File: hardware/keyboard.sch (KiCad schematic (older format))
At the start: 37 parts, among them J1 USB_OTG, J10 PD5, J11 PD6, J12 PD7, J13 PE6, J14 PF0, J15 PF1, J16 PF4, J17 PF5, J18 PF6, J19 PF7, J2 PB5, J3 PB6, J4 PB7, J5 PC6, J6 PC7, J7 PD2, J8 PD3, J9 PD4, U1 ATMEGA32U4-AU, Y1 16MHz

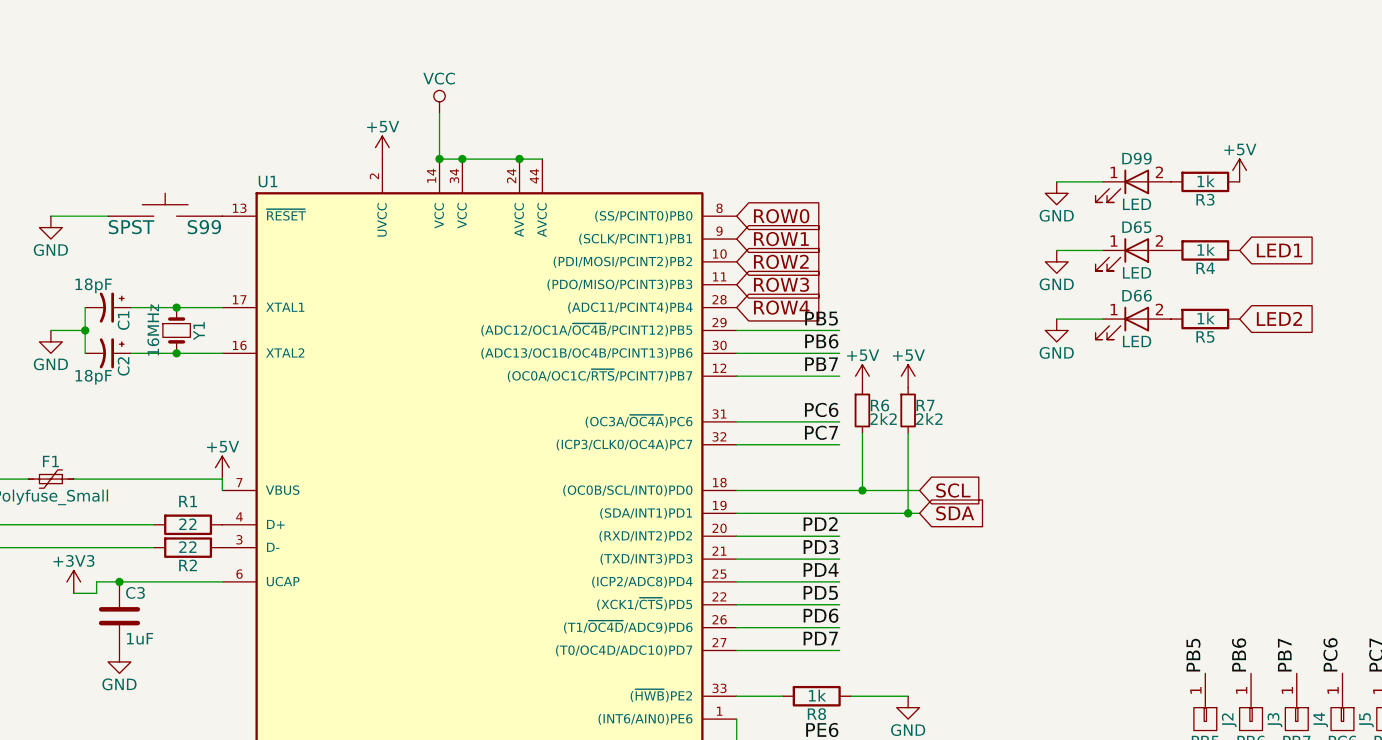
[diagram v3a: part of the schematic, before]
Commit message: Move diodes in script, add big thumb buttons
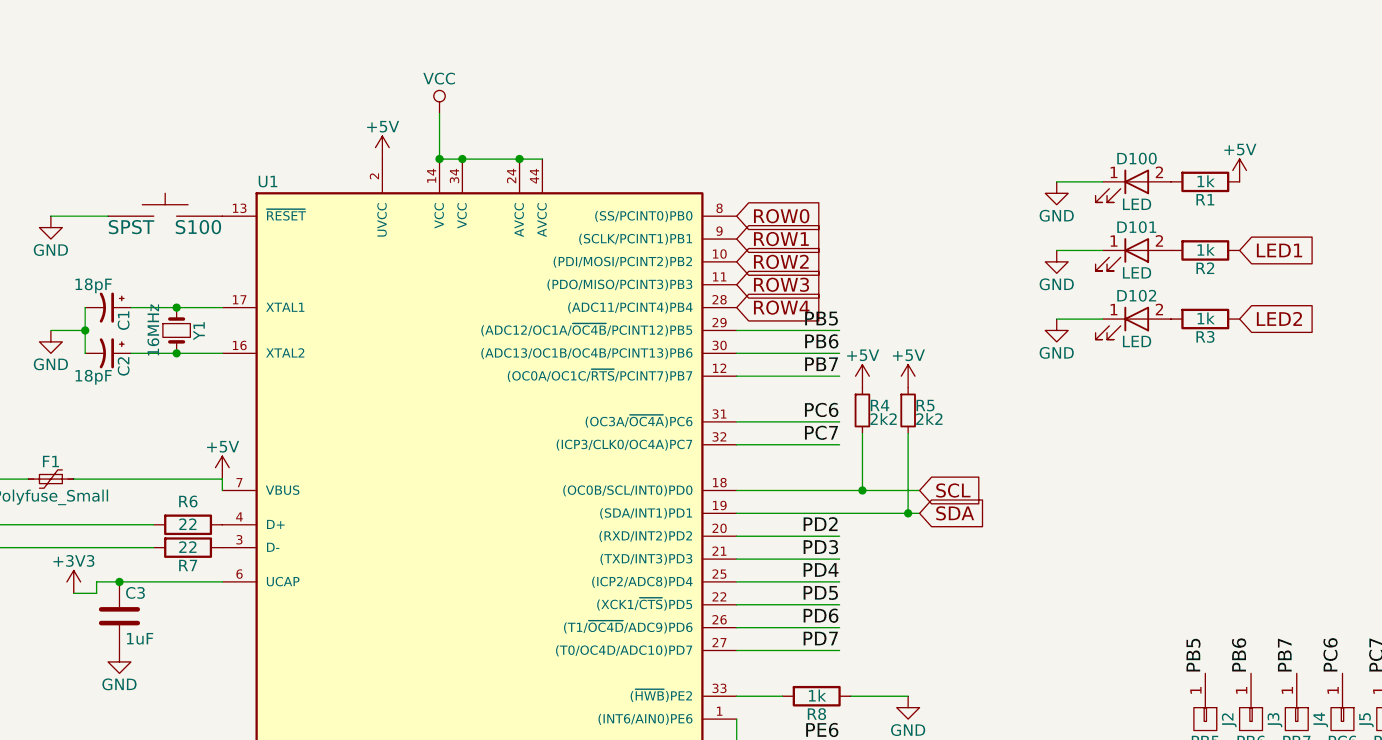
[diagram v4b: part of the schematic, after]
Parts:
- renumbered D99 to D100, D65 to D101, D66 to D102, R3 to R1, R4 to R2, R5 to R3, R6 to R4, R7 to R5, R1 to R6, R2 to R7, S99 to S100
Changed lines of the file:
@@
 $EndComp
 $Comp
-L R R1
+L R R6
 U 1 1 58E91E3A
 P 2650 2700
-F 0 "R1" V 2550 2700 50  0000 C CNN
+F 0 "R6" V 2550 2700 50  0000 C CNN
 F 1 "22" V 2650 2700 50  0000 C CNN
 F 2 "Resistors_SMD:R_1206_HandSoldering" V 2580 2700 50  0001 C CNN
@@
 $EndComp
 $Comp
-L R R2
+L R R7
 U 1 1 58E91EA1
 P 2650 2800
-F 0 "R2" V 2730 2800 50  0000 C CNN
+F 0 "R7" V 2730 2800 50  0000 C CNN
 F 1 "22" V 2650 2800 50  0000 C CNN
 F 2 "Resistors_SMD:R_1206_HandSoldering" V 2580 2800 50  0001 C CNN
@@
 $EndComp
 $Comp
-L LED D99
+L LED D100
 U 1 1 58EC6D5A
 P 6800 1200
-F 0 "D99" H 6800 1300 50  0000 C CNN
+F 0 "D100" H 6800 1300 50  0000 C CNN
 F 1 "LED" H 6800 1100 50  0000 C CNN
 F 2 "LEDs:LED_1206" H 6800 1200 50  0001 C CNN
@@
 $EndComp
 $Comp
-L R R3
+L R R1
 U 1 1 58EC77A9
 P 7100 1200
-F 0 "R3" V 7180 1200 50  0000 C CNN
+F 0 "R1" V 7180 1200 50  0000 C CNN
 F 1 "1k" V 7100 1200 50  0000 C CNN
 F 2 "Resistors_SMD:R_1206_HandSoldering" V 7030 1200 50  0001 C CNN
@@
 	5050 2550 5850 2550
 $Comp
-L R_Small R7
+L R_Small R5
 U 1 1 594E97F5
 P 5800 2200
-F 0 "R7" H 5830 2220 50  0000 L CNN
+F 0 "R5" H 5830 2220 50  0000 L CNN
 F 1 "2k2" H 5830 2160 50  0000 L CNN
 F 2 "Resistors_SMD:R_1206_HandSoldering" H 5800 2200 50  0001 C CNN
@@
 $EndComp
 $Comp
-L R_Small R6
+L R_Small R4
 U 1 1 594E9840
 P 5600 2200
-F 0 "R6" H 5630 2220 50  0000 L CNN
+F 0 "R4" H 5630 2220 50  0000 L CNN
 F 1 "2k2" H 5630 2160 50  0000 L CNN
 F 2 "Resistors_SMD:R_1206_HandSoldering" H 5600 2200 50  0001 C CNN
@@
 $EndComp
 $Comp
-L LED D65
+L LED D101
 U 1 1 594E9DFB
 P 6800 1500
-F 0 "D65" H 6800 1600 50  0000 C CNN
+F 0 "D101" H 6800 1600 50  0000 C CNN
 F 1 "LED" H 6800 1400 50  0000 C CNN
 F 2 "LEDs:LED_1206" H 6800 1500 50  0001 C CNN
@@
 $EndComp
 $Comp
-L R R4
+L R R2
 U 1 1 594E9E0D
 P 7100 1500
-F 0 "R4" V 7180 1500 50  0000 C CNN
+F 0 "R2" V 7180 1500 50  0000 C CNN
 F 1 "1k" V 7100 1500 50  0000 C CNN
 F 2 "Resistors_SMD:R_1206_HandSoldering" V 7030 1500 50  0001 C CNN
@@
 	6650 1500 6450 1500
 $Comp
-L LED D66
+L LED D102
 U 1 1 594E9E7C
 P 6800 1800
-F 0 "D66" H 6800 1900 50  0000 C CNN
+F 0 "D102" H 6800 1900 50  0000 C CNN
 F 1 "LED" H 6800 1700 50  0000 C CNN
 F 2 "LEDs:LED_1206" H 6800 1800 50  0001 C CNN
@@
 $EndComp
 $Comp
-L R R5
+L R R3
 U 1 1 594E9E8E
 P 7100 1800
-F 0 "R5" V 7180 1800 50  0000 C CNN
+F 0 "R3" V 7180 1800 50  0000 C CNN
 F 1 "1k" V 7100 1800 50  0000 C CNN
 F 2 "Resistors_SMD:R_1206_HandSoldering" V 7030 1800 50  0001 C CNN
@@
 $EndComp
 $Comp
-L SPST S99
+L SPST S100
 U 1 1 594EAF2A
 P 2550 1350
-F 0 "S99" H 2800 1300 60  0000 R CNN
+F 0 "S100" H 2800 1300 60  0000 R CNN
 F 1 "SPST" H 2400 1300 60  0000 C CNN
 F 2 "Buttons_Switches_SMD:SW_SPST_EVQP0" H 2550 1450 60  0001 C CNN

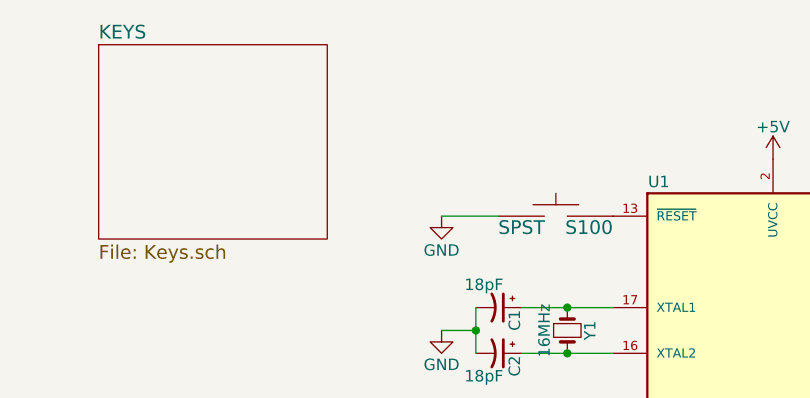
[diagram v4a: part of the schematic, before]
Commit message: Fix diodes, Add board edge
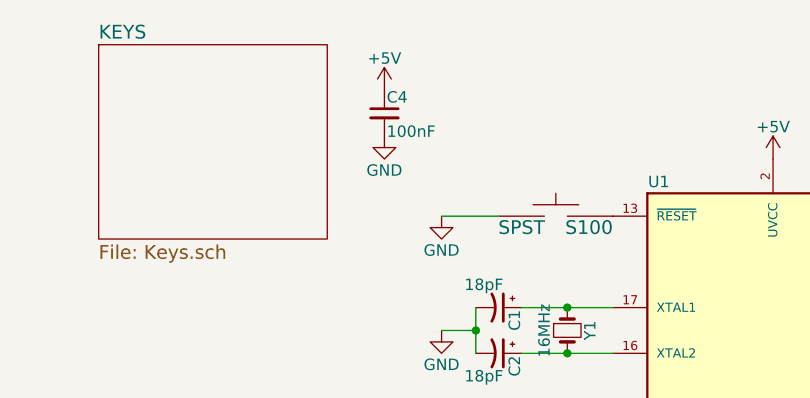
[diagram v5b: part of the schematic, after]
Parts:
- added C4: 100nF, Capacitors_SMD:C_1206_HandSoldering, symbol C_Small
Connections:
- net +5V: now also C4.1
- net GND: now also C4.2
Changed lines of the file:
@@
 $EndDescr
 $Comp
-L GND #PWR01
+L GND #PWR17
 U 1 1 58E84057
 P 3950 4550
-F 0 "#PWR01" H 3950 4300 50  0001 C CNN
+F 0 "#PWR17" H 3950 4300 50  0001 C CNN
 F 1 "GND" H 3950 4400 50  0000 C CNN
 F 2 "" H 3950 4550 50  0001 C CNN
@@
 $EndComp
 $Comp
-L VCC #PWR02
+L VCC #PWR2
 U 1 1 58E840B4
 P 3750 900
-F 0 "#PWR02" H 3750 750 50  0001 C CNN
+F 0 "#PWR2" H 3750 750 50  0001 C CNN
 F 1 "VCC" H 3750 1050 50  0000 C CNN
 F 2 "" H 3750 900 50  0001 C CNN
@@
 $EndComp
 $Comp
-L GND #PWR03
+L GND #PWR15
 U 1 1 58EC68C5
 P 2350 3250
-F 0 "#PWR03" H 2350 3000 50  0001 C CNN
+F 0 "#PWR15" H 2350 3000 50  0001 C CNN
 F 1 "GND" H 2350 3100 50  0000 C CNN
 F 2 "" H 2350 3250 50  0001 C CNN
@@
 $EndComp
 $Comp
-L +3V3 #PWR04
+L +3V3 #PWR14
 U 1 1 58EC69E9
 P 2150 3000
-F 0 "#PWR04" H 2150 2850 50  0001 C CNN
+F 0 "#PWR14" H 2150 2850 50  0001 C CNN
 F 1 "+3V3" H 2150 3140 50  0000 C CNN
 F 2 "" H 2150 3000 50  0001 C CNN
@@
 $EndComp
 $Comp
-L GND #PWR05
+L GND #PWR5
 U 1 1 58EC7101
 P 6450 1200
-F 0 "#PWR05" H 6450 950 50  0001 C CNN
+F 0 "#PWR5" H 6450 950 50  0001 C CNN
 F 1 "GND" H 6450 1050 50  0000 C CNN
 F 2 "" H 6450 1200 50  0001 C CNN
@@
 $EndComp
 $Comp
-L +5V #PWR06
+L +5V #PWR6
 U 1 1 58EC7227
 P 7250 1200
-F 0 "#PWR06" H 7250 1050 50  0001 C CNN
+F 0 "#PWR6" H 7250 1050 50  0001 C CNN
 F 1 "+5V" H 7250 1340 50  0000 C CNN
 F 2 "" H 7250 1200 50  0001 C CNN
@@
 $EndComp
 $Comp
-L GND #PWR07
+L GND #PWR10
 U 1 1 58EC962F
 P 2050 1850
-F 0 "#PWR07" H 2050 1600 50  0001 C CNN
+F 0 "#PWR10" H 2050 1600 50  0001 C CNN
 F 1 "GND" H 2050 1700 50  0000 C CNN
 F 2 "" H 2050 1850 50  0001 C CNN
@@
 $EndComp
 $Comp
-L +5V #PWR08
+L +5V #PWR13
 U 1 1 58ED0C76
 P 2800 2500
-F 0 "#PWR08" H 2800 2350 50  0001 C CNN
+F 0 "#PWR13" H 2800 2350 50  0001 C CNN
 F 1 "+5V" H 2800 2640 50  0000 C CNN
 F 2 "" H 2800 2500 50  0001 C CNN
@@
 $EndComp
 $Comp
-L +5V #PWR09
+L +5V #PWR4
 U 1 1 58ED0DA2
 P 3500 1100
-F 0 "#PWR09" H 3500 950 50  0001 C CNN
+F 0 "#PWR4" H 3500 950 50  0001 C CNN
 F 1 "+5V" H 3500 1240 50  0000 C CNN
 F 2 "" H 3500 1100 50  0001 C CNN
@@
 Connection ~ 5800 2650
 $Comp
-L +5V #PWR010
+L +5V #PWR11
 U 1 1 594E98E9
 P 5600 2100
-F 0 "#PWR010" H 5600 1950 50  0001 C CNN
+F 0 "#PWR11" H 5600 1950 50  0001 C CNN
 F 1 "+5V" H 5600 2240 50  0000 C CNN
 F 2 "" H 5600 2100 50  0001 C CNN
@@
 $EndComp
 $Comp
-L +5V #PWR011
+L +5V #PWR12
 U 1 1 594E9917
 P 5800 2100
-F 0 "#PWR011" H 5800 1950 50  0001 C CNN
+F 0 "#PWR12" H 5800 1950 50  0001 C CNN
 F 1 "+5V" H 5800 2240 50  0000 C CNN
 F 2 "" H 5800 2100 50  0001 C CNN
@@
 $EndComp
 $Comp
-L GND #PWR012
+L GND #PWR8
 U 1 1 594E9E01
 P 6450 1500
-F 0 "#PWR012" H 6450 1250 50  0001 C CNN
+F 0 "#PWR8" H 6450 1250 50  0001 C CNN
 F 1 "GND" H 6450 1350 50  0000 C CNN
 F 2 "" H 6450 1500 50  0001 C CNN
@@
 $EndComp
 $Comp
-L GND #PWR013
+L GND #PWR9
 U 1 1 594E9E82
 P 6450 1800
-F 0 "#PWR013" H 6450 1550 50  0001 C CNN
+F 0 "#PWR9" H 6450 1550 50  0001 C CNN
 F 1 "GND" H 6450 1650 50  0000 C CNN
 F 2 "" H 6450 1800 50  0001 C CNN
@@
 	5050 3450 5250 3450
 $Comp
-L GND #PWR014
+L GND #PWR16
 U 1 1 594EA1C7
 P 5800 3450
-F 0 "#PWR014" H 5800 3200 50  0001 C CNN
+F 0 "#PWR16" H 5800 3200 50  0001 C CNN
 F 1 "GND" H 5800 3300 50  0000 C CNN
 F 2 "" H 5800 3450 50  0001 C CNN
@@
 	5550 3450 5800 3450
 $Comp
-L GND #PWR015
+L GND #PWR7
 U 1 1 594EA3EB
 P 2050 1350
-F 0 "#PWR015" H 2050 1100 50  0001 C CNN
+F 0 "#PWR7" H 2050 1100 50  0001 C CNN
 F 1 "GND" H 2050 1200 50  0000 C CNN
 F 2 "" H 2050 1350 50  0001 C CNN
@@
 Text Label 8300 3900 1    60   ~ 0
 PF5
+$Comp
+L C_Small C4
+U 1 1 5955BBCD
+P 1800 900
+F 0 "C4" H 1810 970 50  0000 L CNN
+F 1 "100nF" H 1810 820 50  0000 L CNN
+F 2 "Capacitors_SMD:C_1206_HandSoldering" H 1800 900 50  0001 C CNN
+F 3 "" H 1800 900 50  0001 C CNN
+	1    1800 900
+	1    0    0    -1
+$EndComp
+$Comp
+L +5V #PWR1
+U 1 1 5955BD4A
+P 1800 800
+F 0 "#PWR1" H 1800 650 50  0001 C CNN
+F 1 "+5V" H 1800 940 50  0000 C CNN
+F 2 "" H 1800 800 50  0001 C CNN
+F 3 "" H 1800 800 50  0001 C CNN
+	1    1800 800
+	1    0    0    -1
+$EndComp
+$Comp
+L GND #PWR3
+U 1 1 5955BE42
+P 1800 1000
+F 0 "#PWR3" H 1800 750 50  0001 C CNN
+F 1 "GND" H 1800 850 50  0000 C CNN
+F 2 "" H 1800 1000 50  0001 C CNN
+F 3 "" H 1800 1000 50  0001 C CNN
+	1    1800 1000
+	1    0    0    -1
+$EndComp
 $EndSCHEMATC

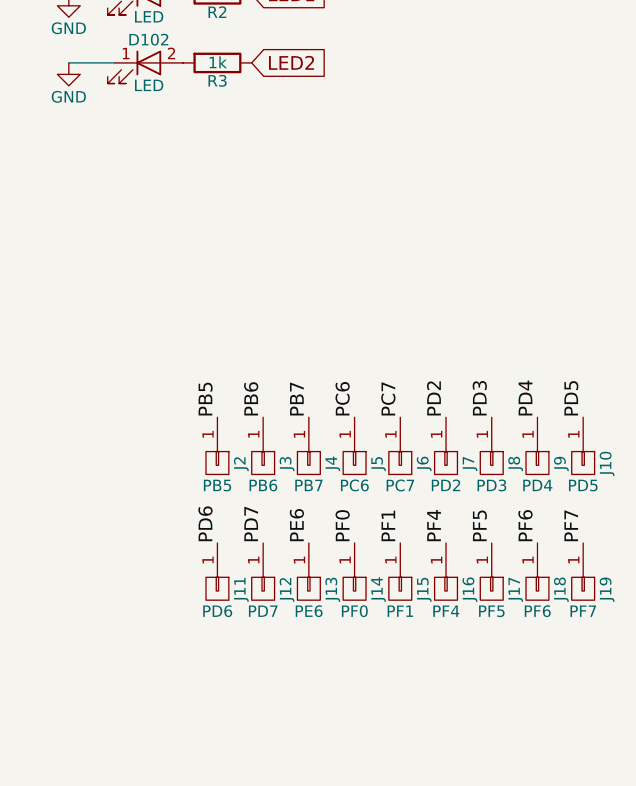
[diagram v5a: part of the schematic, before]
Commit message: Update expansion pads to be SMD
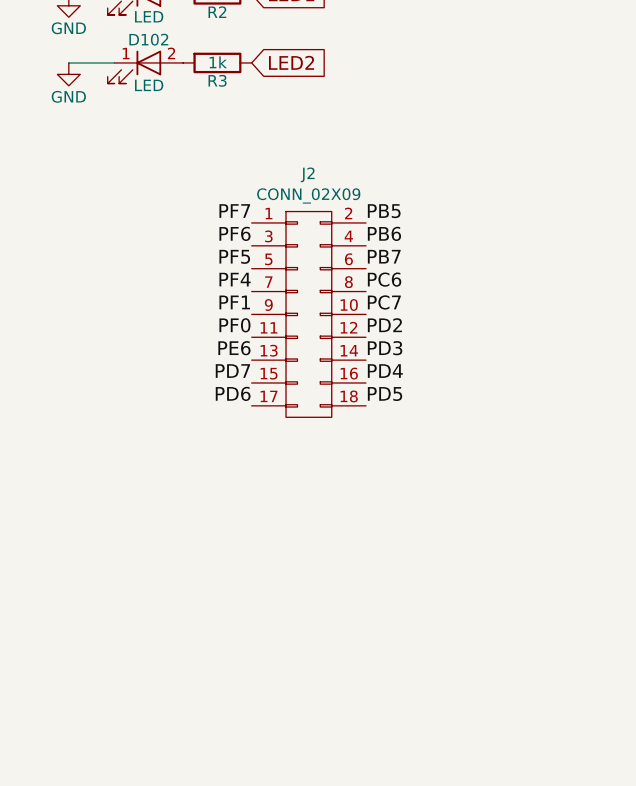
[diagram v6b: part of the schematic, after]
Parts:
- removed J10: PD5, Connectors:1pin, symbol CONN_01X01
- removed J11: PD6, Connectors:1pin, symbol CONN_01X01
- removed J12: PD7, Connectors:1pin, symbol CONN_01X01
- removed J13: PE6, Connectors:1pin, symbol CONN_01X01
- removed J14: PF0, Connectors:1pin, symbol CONN_01X01
- removed J15: PF1, Connectors:1pin, symbol CONN_01X01
- removed J16: PF4, Connectors:1pin, symbol CONN_01X01
- removed J17: PF5, Connectors:1pin, symbol CONN_01X01
- removed J18: PF6, Connectors:1pin, symbol CONN_01X01
- removed J19: PF7, Connectors:1pin, symbol CONN_01X01
- removed J2: PB5, Connectors:1pin, symbol CONN_01X01
- removed J3: PB6, Connectors:1pin, symbol CONN_01X01
- removed J4: PB7, Connectors:1pin, symbol CONN_01X01
- removed J5: PC6, Connectors:1pin, symbol CONN_01X01
- removed J6: PC7, Connectors:1pin, symbol CONN_01X01
- removed J7: PD2, Connectors:1pin, symbol CONN_01X01
- removed J8: PD3, Connectors:1pin, symbol CONN_01X01
- removed J9: PD4, Connectors:1pin, symbol CONN_01X01
- added J2: CONN_02X09, keyboard-modules:pads, symbol CONN_02X09
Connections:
- net PB5: now also J2.2 (P2)
- net PB6: now also J2.4 (P4)
- net PB7: now also J2.6 (P6)
- net PC6: now also J2.8 (P8)
- net PC7: now also J2.10 (P10)
- net PD2: now also J2.12 (P12)
- net PD3: now also J2.14 (P14)
- net PD4: now also J2.16 (P16)
- net PD5: now also J2.18 (P18)
- net PD6: now also J2.17 (P17)
- net PD7: now also J2.15 (P15)
- net PE6: now also J2.13 (P13)
- net PF0: now also J2.11 (P11)
- net PF1: now also J2.9 (P9)
- net PF4: now also J2.7 (P7)
- net PF5: now also J2.5 (P5)
- net PF6: now also J2.3 (P3)
- net PF7: now also J2.1 (P1)
